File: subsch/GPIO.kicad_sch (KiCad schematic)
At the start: 10 parts, among them U10 PCF8574, U9 ATtiny85V-10S

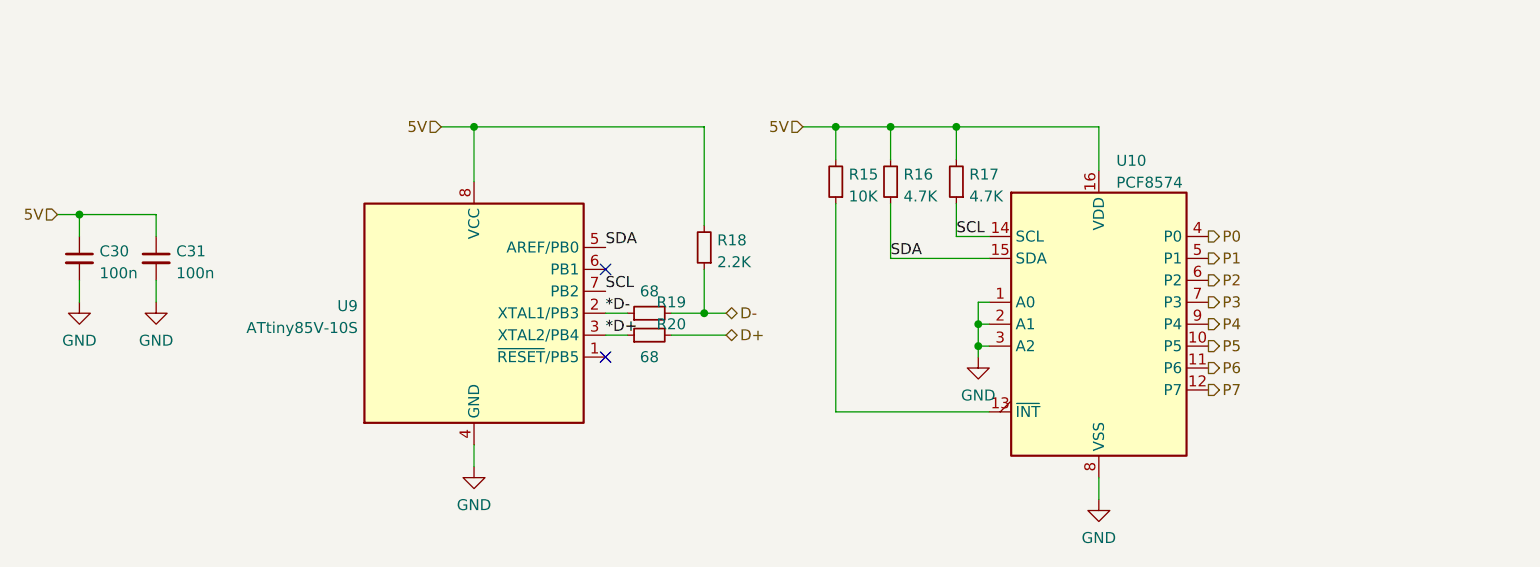
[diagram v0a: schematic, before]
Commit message: Change routings&Add ESD for UART and CAN&Add 5V protection and pull-resistance for GPIO
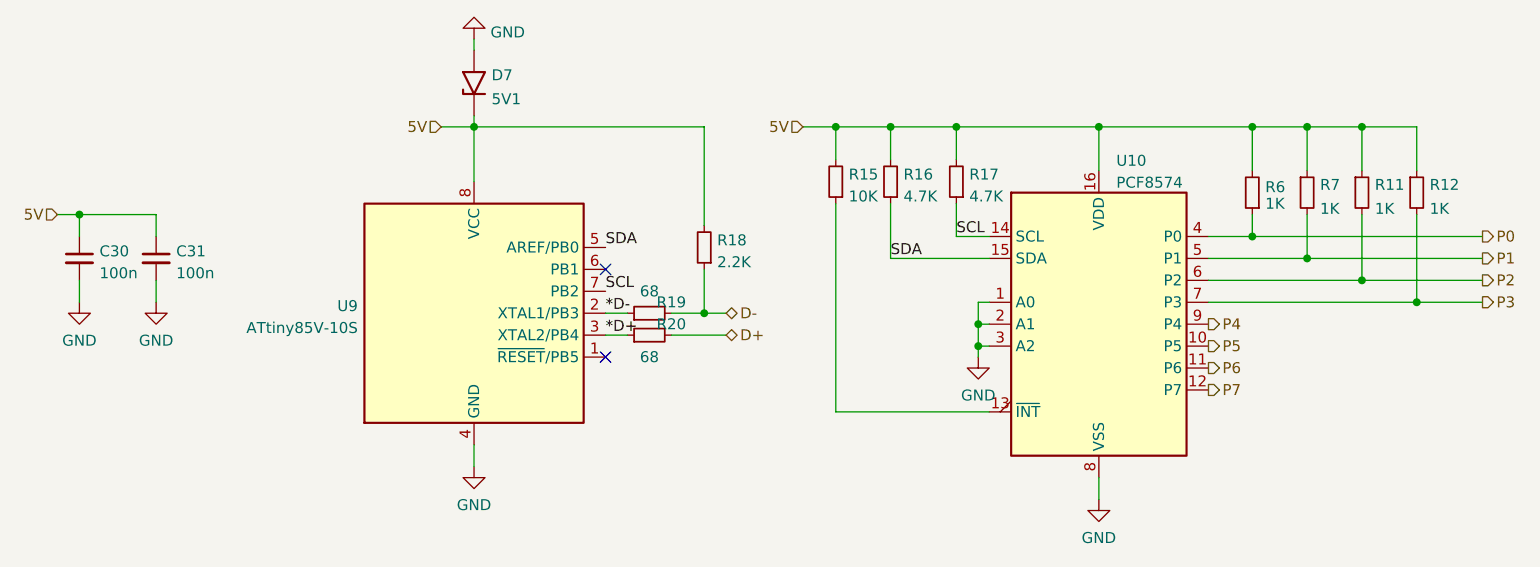
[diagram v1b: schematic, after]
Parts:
- added D7: 5V1, Diode_SMD:D_SOD-123, symbol Diode:1N630xA
- added R11, R12, R6, R7: 1K, Resistor_SMD:R_0603_1608Metric, symbol Device:R_Small
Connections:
- net 5V: now also D7.1 (A1), R11.1, R12.1, R6.2, R7.1
- net GND: now also D7.2 (A2)
- net P0: now also R6.1
- net P1: now also R7.2
- net P2: now also R11.2
- net P3: now also R12.2
